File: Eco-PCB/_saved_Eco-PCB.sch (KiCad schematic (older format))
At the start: 14 parts, among them J1 DB25_Female, M1 SD Card, M1_1 XSOURCE Wireless, P1 Power_Block

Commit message: Pcb 1 design done V1.0
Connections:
- net CS_: now also Master1.13 (D10); no longer Master1.12 (D9)
- net SCK: now also Master1.16 (D13); no longer Master1.13 (D10)
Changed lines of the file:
@@
 	8900 1000 8900 1100
-Wire Wire Line
-	5800 2700 6000 2700
-Wire Wire Line
-	6000 2700 6000 5500
-Wire Wire Line
-	5800 2600 6100 2600
-Wire Wire Line
-	6100 2600 6100 5400
 Wire Wire Line
 	6950 1800 7100 1800
@@
 Wire Wire Line
 	6450 3050 6450 3700
+Wire Wire Line
+	6100 2700 6100 5400
+Wire Wire Line
+	6000 3000 5800 3000
+Wire Wire Line
+	6000 3000 6000 5500
+Wire Wire Line
+	5800 2700 6100 2700
 $EndSCHEMATC

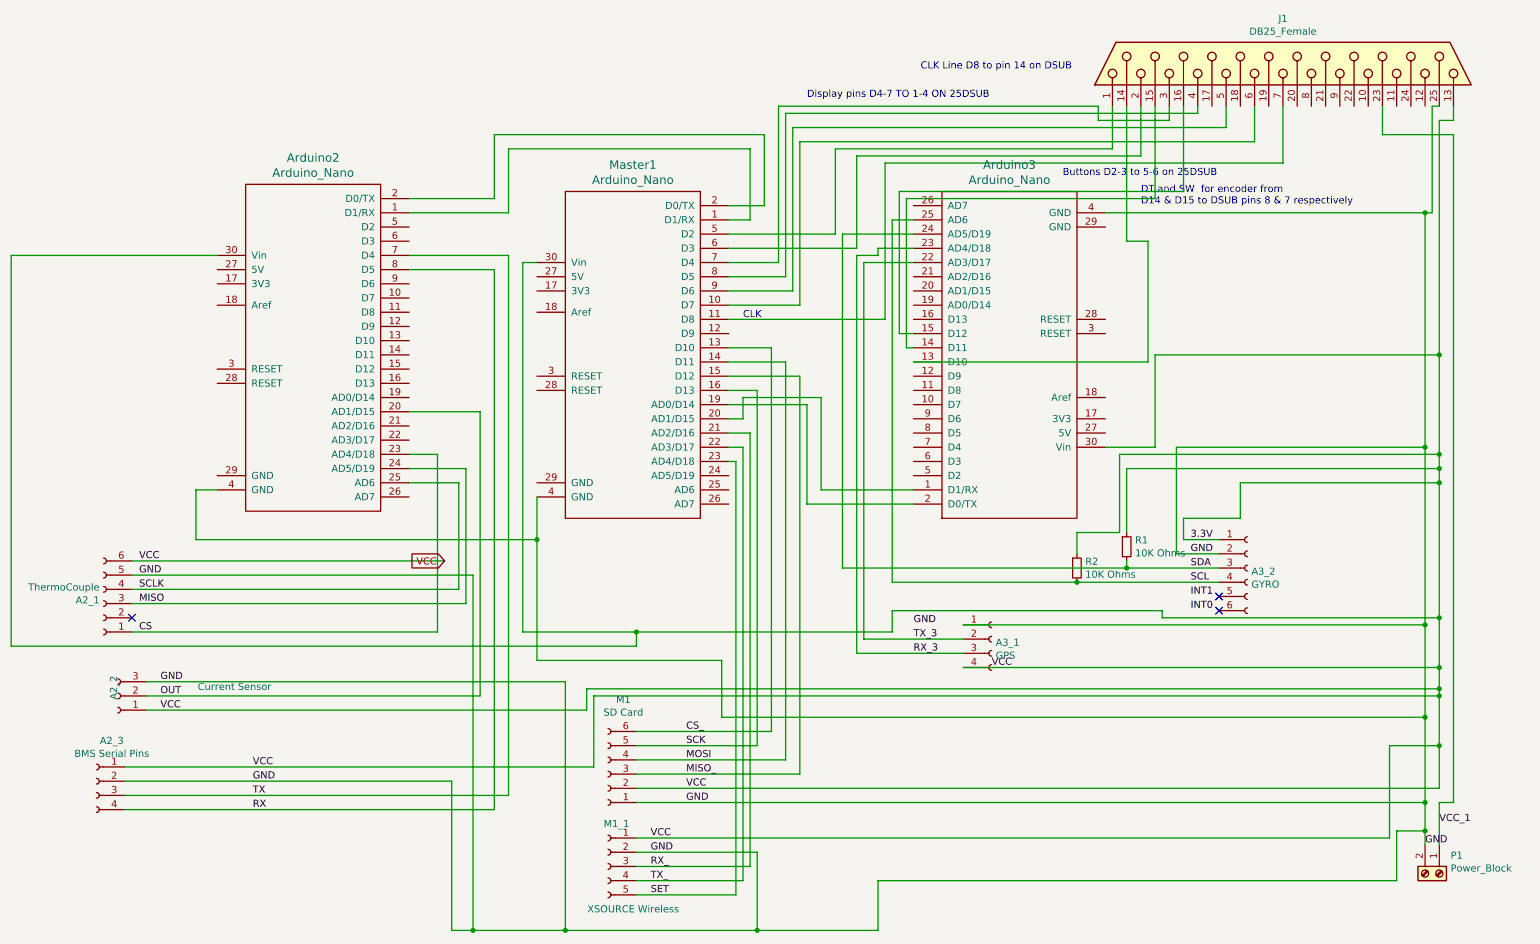
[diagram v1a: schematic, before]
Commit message: PCB1 added CLK line & PCB2 Design done
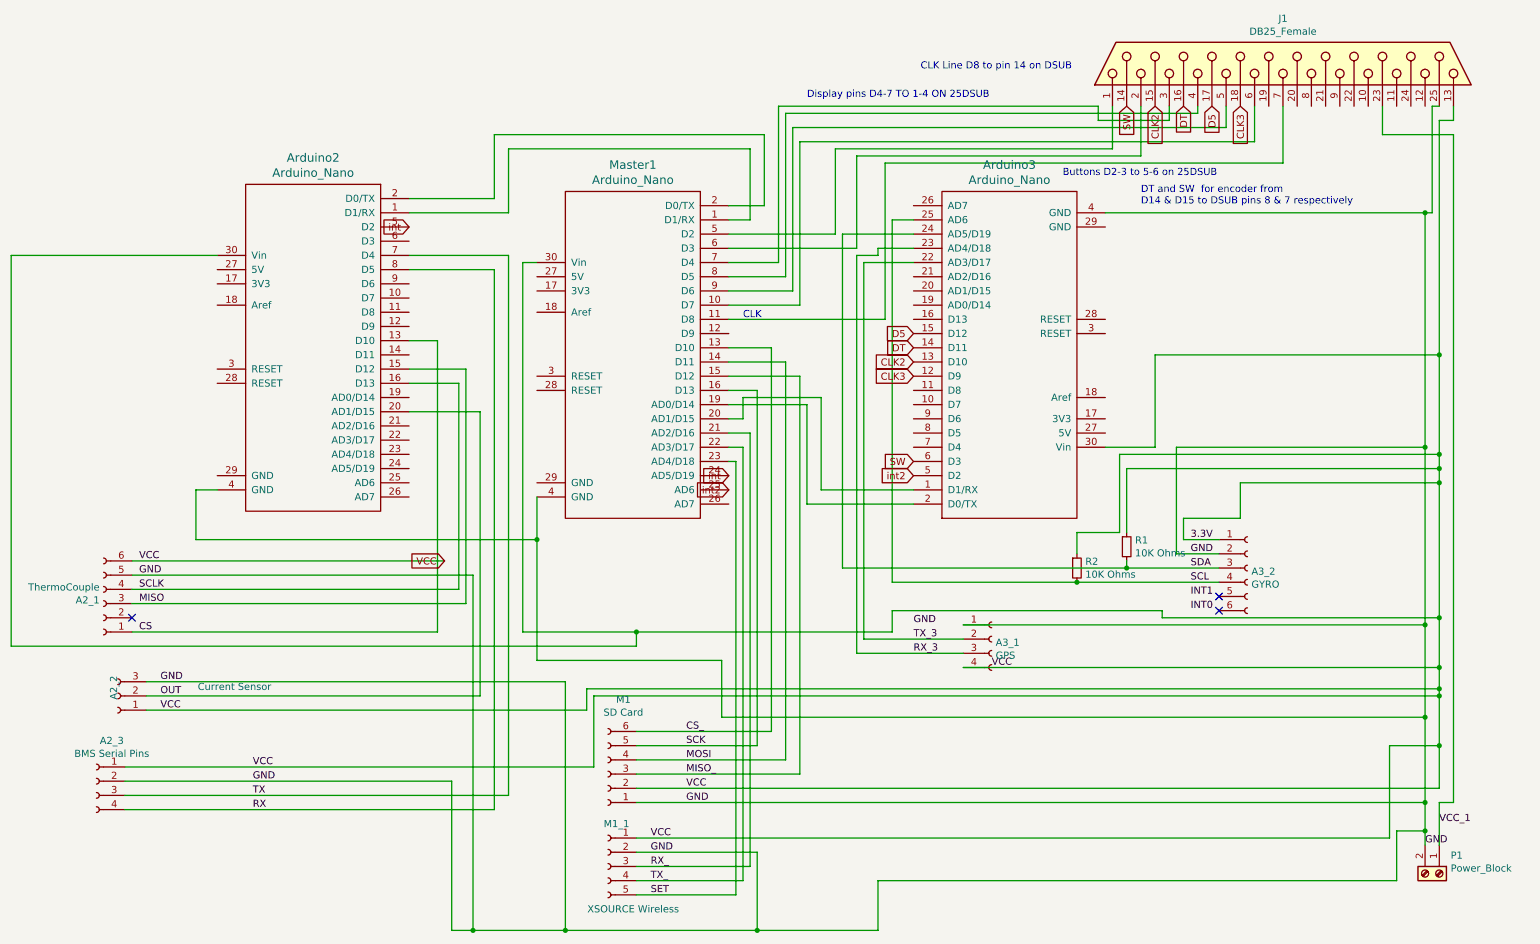
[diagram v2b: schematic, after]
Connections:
- net CS: now also Arduino2.13 (D10); no longer Arduino2.23 (AD4/D18)
- net MISO: now also Arduino2.15 (D12); no longer Arduino2.24 (AD5/D19)
- net SCLK: now also Arduino2.16 (D13); no longer Arduino2.25 (AD6)
- net int: now reaches Arduino2.5 (D2)
- net int: now also Master1.24 (AD5/D19)
- net int2: now reaches Master1.25 (AD6)
- net int2: now also Arduino3.5 (D2)
- net CLK3: now reaches Arduino3.12 (D9)
- net CLK3: now also J1.18 (P18)
- net CLK2: now reaches Arduino3.13 (D10)
- net CLK2: now also J1.15 (P15); no longer J1.14 (P14)
- net DT: now reaches Arduino3.14 (D11)
- net DT: now also J1.16 (P16); no longer J1.15 (P15)
- net D5: now reaches Arduino3.15 (D12)
- net D5: now also J1.17 (P17); no longer J1.16 (P16)
- net SW: now reaches Arduino3.6 (D3)
- net SW: now also J1.14 (P14)
